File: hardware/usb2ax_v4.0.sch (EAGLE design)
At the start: 36 parts, among them U1 IC_LPC11U14FET48/201, U2 IPC4282CZ6, U3 LD6805K/33P, U4 TPS71550DCKR or MIC5213-5.0YC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, U5 SN74AHC1G125DCKR, U6 SI8631EC-B-IS1, X1 CRYSTAL-306010047 12Mhz

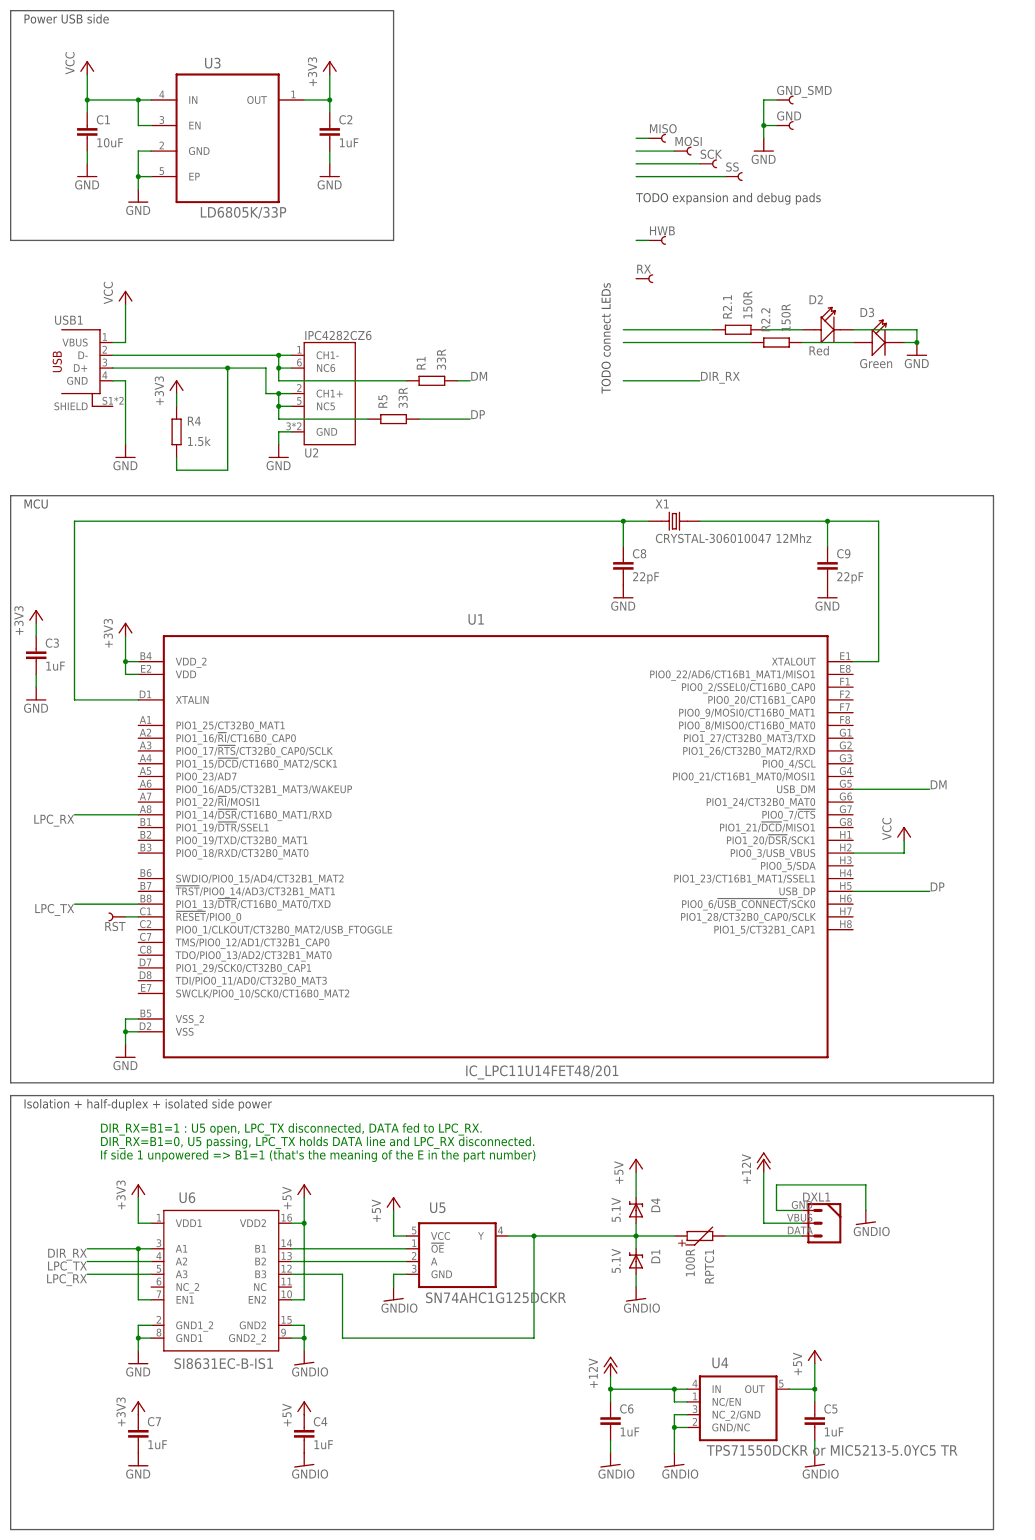
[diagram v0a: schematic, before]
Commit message: v4 hardware: sch probably done, tentative routing.
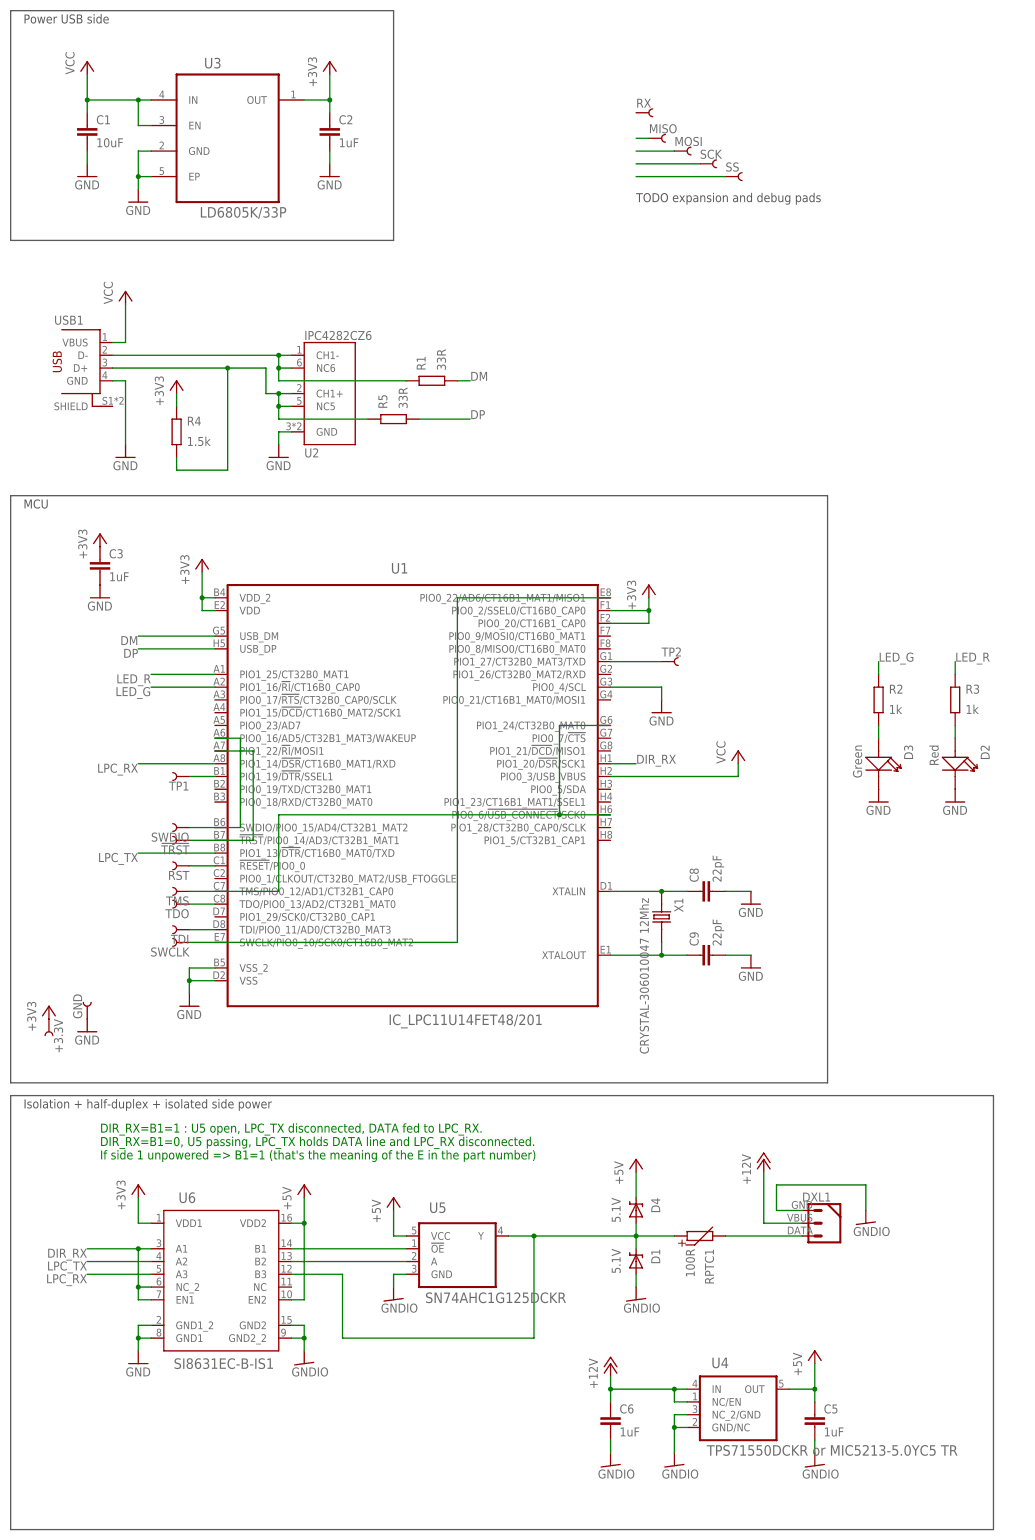
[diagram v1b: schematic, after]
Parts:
- removed C4, C7: 1uF, Xevelabs:C0402
- removed GND_SMD, HWB: PIN_SMD_2X2.5, Xevelabs:PIN_SMD_2X2.5
- added !TRST, +3.3V, SWCLK, SWDIO, TDI, TDO, TMS, TP1, TP2: PIN_SMD_1X1, Xevelabs:PIN_SMD_1X1
- added R3: 1k, Xevelabs:R0201
- GND, RST: value PIN_SMD_2X2.5 -> PIN_SMD_1X1; device Xevelabs:PIN_SMD_2X2.5 -> Xevelabs:PIN_SMD_1X1
- R2: value 150R -> 1k; device Xevelabs:R_2-0402 -> Xevelabs:R0201
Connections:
- removed net HWB: HWB.1
- removed net N$13: D2.+, R2.1.1
- removed net N$14: D3.+, R2.2.1
- removed net N$15: R2.1.2
- new net !TRST: !TRST.1, U1.!TRST!/PIO0_14/AD3/CT32B1_MAT1, U1.PIO1_22/!RI!/MOSI1
- new net LED_G: R2.2, U1.PIO1_16/!RI!/CT16B0_CAP0
- new net LED_R: R3.2, U1.PIO1_25/CT32B0_MAT1
- new net N$1: TP1.1, U1.PIO1_19/!DTR!/SSEL1
- new net N$2: D3.+, R2.1
- new net N$9: D2.+, R3.1
- new net SWCLK: SWCLK.1, U1.PIO0_22/AD6/CT16B1_MAT1/MISO1, U1.SWCLK/PIO0_10/SCK0/CT16B0_MAT2
- new net SWDIO: SWDIO.1, U1.PIO0_16/AD5/CT32B1_MAT3/WAKEUP, U1.SWDIO/PIO0_15/AD4/CT32B1_MAT2
- new net TDI: TDI.1, U1.TDI/PIO0_11/AD0/CT32B0_MAT3
- new net TDO: TDO.1, U1.TDO/PIO0_13/AD2/CT32B1_MAT0
- new net TMS: TMS.1, U1.PIO0_6/!USB_CONNECT!/SCK0, U1.PIO1_24/CT32B0_MAT0, U1.TMS/PIO0_12/AD1/CT32B1_CAP0
- net +3V3: now also +3.3V.1, U1.PIO0_2/SSEL0/CT16B0_CAP0, U1.PIO0_20/CT16B1_CAP0; no longer C7.1
- net +5V: no longer C4.1
- net DIR_RX: now also U1.PIO1_20/!DSR!/SCK1, U6.NC_2
- net GND: now also U1.PIO0_4/SCL; no longer C7.2, GND_SMD.1
- net GNDIO: no longer C4.2
- net N$5: now also TP2.1, U1.PIO1_27/CT32B0_MAT3/TXD; no longer R2.2.2
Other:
- note removed: "TODO connect LEDs"
- moved on the sheet: C3, C8, C9, D2, D3, GND, RST, RX, U1, X1

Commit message: v4 hardware probably done.
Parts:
- removed MISO, MOSI, SCK, SS: PIN_SMD_2X2.5, Xevelabs:PIN_SMD_2X2.5
- removed RX: PIN_THT_0.8, Xevelabs:PIN_THT_0.8
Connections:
- removed net N$17: MISO.1
- removed net N$18: MOSI.1
- removed net N$19: SCK.1
- removed net N$20: SS.1
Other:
- note removed: "TODO expansion and debug pads"
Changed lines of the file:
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@@
 <grid distance="0.1" unitdist="inch" unit="inch" style="lines" multiple="1" display="no" altdistance="0.01" altunitdist="inch" altunit="inch"/>
 <layers>
-<layer number="1" name="Top" color="4" fill="1" visible="yes" active="no"/>
-<layer number="2" name="Route2" color="1" fill="3" visible="yes" active="no"/>
-<layer number="3" name="Route3" color="4" fill="3" visible="yes" active="no"/>
-<layer number="14" name="Route14" color="1" fill="6" visible="yes" active="no"/>
-<layer number="15" name="Route15" color="4" fill="6" visible="yes" active="no"/>
-<layer number="16" name="Bottom" color="1" fill="1" visible="yes" active="no"/>
-<layer number="17" name="Pads" color="2" fill="1" visible="yes" active="no"/>
-<layer number="18" name="Vias" color="2" fill="1" visible="yes" active="no"/>
-<layer number="19" name="Unrouted" color="6" fill="1" visible="yes" active="no"/>
-<layer number="20" name="Dimension" color="15" fill="1" visible="yes" active="no"/>
-<layer number="21" name="tPlace" color="7" fill="1" visible="yes" active="no"/>
-<layer number="22" name="bPlace" color="7" fill="1" visible="yes" active="no"/>
-<layer number="23" name="tOrigins" color="15" fill="1" visible="yes" active="no"/>
-<layer number="24" name="bOrigins" color="15" fill="1" visible="yes" active="no"/>
-<layer number="25" name="tNames" color="7" fill="1" visible="yes" active="no"/>
-<layer number="26" name="bNames" color="7" fill="1" visible="yes" active="no"/>
-<layer number="27" name="tValues" color="7" fill="1" visible="yes" active="no"/>
-<layer number="28" name="bValues" color="7" fill="1" visible="yes" active="no"/>
+<layer number="1" name="Top" color="4" fill="1" visible="no" active="no"/>
+<layer number="2" name="Route2" color="1" fill="3" visible="no" active="no"/>
+<layer number="3" name="Route3" color="4" fill="3" visible="no" active="no"/>
+<layer number="14" name="Route14" color="1" fill="6" visible="no" active="no"/>
+<layer number="15" name="Route15" color="4" fill="6" visible="no" active="no"/>
+<layer number="16" name="Bottom" color="1" fill="1" visible="no" active="no"/>
+<layer number="17" name="Pads" color="2" fill="1" visible="no" active="no"/>
+<layer number="18" name="Vias" color="2" fill="1" visible="no" active="no"/>
+<layer number="19" name="Unrouted" color="6" fill="1" visible="no" active="no"/>
+<layer number="20" name="Dimension" color="15" fill="1" visible="no" active="no"/>
+<layer number="21" name="tPlace" color="7" fill="1" visible="no" active="no"/>
+<layer number="22" name="bPlace" color="7" fill="1" visible="no" active="no"/>
+<layer number="23" name="tOrigins" color="15" fill="1" visible="no" active="no"/>
+<layer number="24" name="bOrigins" color="15" fill="1" visible="no" active="no"/>
+<layer number="25" name="tNames" color="7" fill="1" visible="no" active="no"/>
+<layer number="26" name="bNames" color="7" fill="1" visible="no" active="no"/>
+<layer number="27" name="tValues" color="7" fill="1" visible="no" active="no"/>
+<layer number="28" name="bValues" color="7" fill="1" visible="no" active="no"/>
 <layer number="29" name="tStop" color="7" fill="3" visible="no" active="no"/>
 <layer number="30" name="bStop" color="7" fill="6" visible="no" active="no"/>
@@
 <layer number="35" name="tGlue" color="7" fill="4" visible="no" active="no"/>
 <layer number="36" name="bGlue" color="7" fill="5" visible="no" active="no"/>
-<layer number="37" name="tTest" color="7" fill="1" visible="yes" active="no"/>
-<layer number="38" name="bTest" color="7" fill="1" visible="yes" active="no"/>
+<layer number="37" name="tTest" color="7" fill="1" visible="no" active="no"/>
+<layer number="38" name="bTest" color="7" fill="1" visible="no" active="no"/>
 <layer number="39" name="tKeepout" color="4" fill="11" visible="no" active="no"/>
 <layer number="40" name="bKeepout" color="1" fill="11" visible="no" active="no"/>
@@
 <layer number="44" name="Drills" color="7" fill="1" visible="no" active="no"/>
 <layer number="45" name="Holes" color="7" fill="1" visible="no" active="no"/>
-<layer number="46" name="Milling" color="3" fill="1" visible="yes" active="no"/>
-<layer number="47" name="Measures" color="7" fill="1" visible="yes" active="no"/>
-<layer number="48" name="Document" color="7" fill="1" visible="yes" active="no"/>
-<layer number="49" name="Reference" color="7" fill="1" visible="yes" active="no"/>
-<layer number="50" name="dxf" color="7" fill="1" visible="yes" active="no"/>
-<layer number="51" name="tDocu" color="13" fill="1" visible="yes" active="no"/>
-<layer number="52" name="bDocu" color="7" fill="1" visible="yes" active="no"/>
-<layer number="53" name="tGND_GNDA" color="7" fill="9" visible="yes" active="no"/>
-<layer number="54" name="bGND_GNDA" color="1" fill="9" visible="yes" active="no"/>
-<layer number="56" name="wert" color="7" fill="1" visible="yes" active="no"/>
+<layer number="46" name="Milling" color="3" fill="1" visible="no" active="no"/>
+<layer number="47" name="Measures" color="7" fill="1" visible="no" active="no"/>
+<layer number="48" name="Document" color="7" fill="1" visible="no" active="no"/>
+<layer number="49" name="Reference" color="7" fill="1" visible="no" active="no"/>
+<layer number="50" name="dxf" color="7" fill="1" visible="no" active="no"/>
+<layer number="51" name="tDocu" color="13" fill="1" visible="no" active="no"/>
+<layer number="52" name="bDocu" color="7" fill="1" visible="no" active="no"/>
+<layer number="53" name="tGND_GNDA" color="7" fill="9" visible="no" active="no"/>
+<layer number="54" name="bGND_GNDA" color="1" fill="9" visible="no" active="no"/>
+<layer number="56" name="wert" color="7" fill="1" visible="no" active="no"/>
 <layer number="90" name="Modules" color="5" fill="1" visible="yes" active="yes"/>
 <layer number="91" name="Nets" color="2" fill="1" visible="yes" active="yes"/>
@@
 <part name="GND9" library="supply1" deviceset="GND" device=""/>
 <part name="DXL1" library="Xevelabs" deviceset="DYNAMIXEL_3POS" device="-R"/>
-<part name="RX" library="Xevelabs" deviceset="PIN" device="_THT_0.8"/>
 <part name="RST" library="Xevelabs" deviceset="PIN" device="_SMD_1X1" value="PIN_SMD_1X1"/>
-<part name="MISO" library="Xevelabs" deviceset="PIN" device="_SMD_2X2.5"/>
-<part name="MOSI" library="Xevelabs" deviceset="PIN" device="_SMD_2X2.5"/>
-<part name="SCK" library="Xevelabs" deviceset="PIN" device="_SMD_2X2.5"/>
-<part name="SS" library="Xevelabs" deviceset="PIN" device="_SMD_2X2.5"/>
 <part name="GND11" library="supply1" deviceset="GND" device=""/>
 <part name="GND" library="Xevelabs" deviceset="PIN" device="_SMD_1X1" value="PIN_SMD_1X1"/>
@@
 <sheet>
 <plain>
-<text x="124.46" y="264.16" size="1.778" layer="92">TODO expansion and debug pads</text>
 <text x="17.78" y="73.66" size="1.778" layer="91">DIR_RX=B1=1 : U5 open, LPC_TX disconnected, DATA fed to LPC_RX.
 DIR_RX=B1=0, U5 passing, LPC_TX holds DATA line and LPC_RX disconnected.
@@
 <instance part="GND9" gate="1" x="22.86" y="213.36"/>
 <instance part="DXL1" gate="G$1" x="160.02" y="60.96"/>
-<instance part="RX" gate="G$1" x="124.46" y="281.94"/>
 <instance part="RST" gate="G$1" x="35.56" y="132.08" rot="R180"/>
-<instance part="MISO" gate="G$1" x="127" y="276.86"/>
-<instance part="MOSI" gate="G$1" x="132.08" y="274.32"/>
-<instance part="SCK" gate="G$1" x="137.16" y="271.78"/>
-<instance part="SS" gate="G$1" x="142.24" y="269.24"/>
 <instance part="GND11" gate="1" x="15.24" y="99.06"/>
 <instance part="GND" gate="G$1" x="15.24" y="101.6" rot="R90"/>
@@
 </segment>
 </net>
-<net name="N$17" class="0">
-<segment>
-<wire x1="124.46" y1="276.86" x2="127" y2="276.86" width="0.1524" layer="91"/>
-<pinref part="MISO" gate="G$1" pin="1"/>
-</segment>
-</net>
-<net name="N$18" class="0">
-<segment>
-<wire x1="124.46" y1="274.32" x2="132.08" y2="274.32" width="0.1524" layer="91"/>
-<pinref part="MOSI" gate="G$1" pin="1"/>
-</segment>
-</net>
-<net name="N$19" class="0">
-<segment>
-<wire x1="124.46" y1="271.78" x2="137.16" y2="271.78" width="0.1524" layer="91"/>
-<pinref part="SCK" gate="G$1" pin="1"/>
-</segment>
-</net>
-<net name="N$20" class="0">
-<segment>
-<wire x1="124.46" y1="269.24" x2="142.24" y2="269.24" width="0.1524" layer="91"/>
-<pinref part="SS" gate="G$1" pin="1"/>
-</segment>
-</net>
